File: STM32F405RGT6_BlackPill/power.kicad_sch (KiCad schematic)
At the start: 12 parts, among them U3 TLV62569DBV

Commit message: Essential part of the BOM fill
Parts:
- C300: renamed from C17; LCSC link https://www.lcsc.com/product-detail/Multilayer-Ceramic-Capa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 -> (none); Manufacturer Samwha Capacitor -> (none); Manufacturer Part Number CS1608Y5V105Z160NRB -> (none)
- C301: renamed from C18; LCSC link https://www.lcsc.com/product-detail/Multilayer-Ceramic-Capa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 -> (none); Manufacturer Samwha Capacitor -> (none); Manufacturer Part Number CS1608Y5V105Z160NRB -> (none)
- C302: renamed from C19; LCSC link https://www.lcsc.com/product-detail/Multilayer-Ceramic-Capa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 -> (none); Manufacturer Samwha Capacitor -> (none); Manufacturer Part Number CS2012X5R226M160NRE -> (none)
- C303: renamed from C22; LCSC link https://www.lcsc.com/product-detail/Multilayer-Ceramic-Capa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 -> (none); Manufacturer Samwha Capacitor -> (none); Manufacturer Part Number CS2012X5R226M160NRE -> (none)
- C304: renamed from C23; now not fitted
- D300: renamed from D4; value GREEN -> LED; LCSC link https://www.lcsc.com/product-detail/LED-Indication-Discrete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 -> (none); Manufacturer Amicc -> (none); Manufacturer Part Number A-SP192DGHC-C01-4T -> (none)
- L300: renamed from L3; footprint Capacitor_SMD:C_0402_1005Metric -> Inductor_SMD:L_0402_1005Metric; LCSC link https://www.lcsc.com/product-detail/Multilayer-Ceramic-Capa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 -> (none); Manufacturer TDK -> (none); Manufacturer Part Number CGA2B3X7R1H103M050BE -> (none)
- L301: renamed from L4; footprint PhilsLab_Footprints_KiCad6:MWSA0603S -> BlackPill:MWSA0603S; DigiKey Part Number (none) -> 3442-MWSA0603S-150MTDKR-ND; LCSC link https://www.lcsc.com/product-detail/Power-Inductors_Sunlord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 -> (none); Manufacturer Sunlord -> Shenzhen Sunlord Electronics Co., Ltd.; Manufacturer Part Number MWSA0603S-150MT -> (none); Manufacturer Product Number (none) -> MWSA0603S-150MT
- R300: renamed from R10; LCSC link https://www.lcsc.com/product-detail/Chip-Resistor-Surface-M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 -> (none); Manufacturer UNI-ROYAL(Uniroyal Elec) -> (none); Manufacturer Part Number 0402WGJ0104TCE -> (none)
- R301: renamed from R11; LCSC link https://www.lcsc.com/product-detail/Chip-Resistor-Surface-M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 -> (none); Manufacturer UNI-ROYAL(Uniroyal Elec) -> (none); Manufacturer Part Number 0402WGF2202TCE -> (none)
- R302: renamed from R12; LCSC link https://www.lcsc.com/product-detail/Chip-Resistor-Surface-M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 -> (none); Manufacturer UNI-ROYAL(Uniroyal Elec) -> (none); Manufacturer Part Number 0402WGF1001TCE -> (none)
- U300: renamed from U3; DigiKey Part Number (none) -> 296-47360-6-ND; LCSC link https://www.lcsc.com/product-detail/DC-DC-Converters_Texas-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 -> (none); Manufacturer Part Number TLV62569DBVR -> (none); Manufacturer Product Number (none) -> TLV62569DBVR

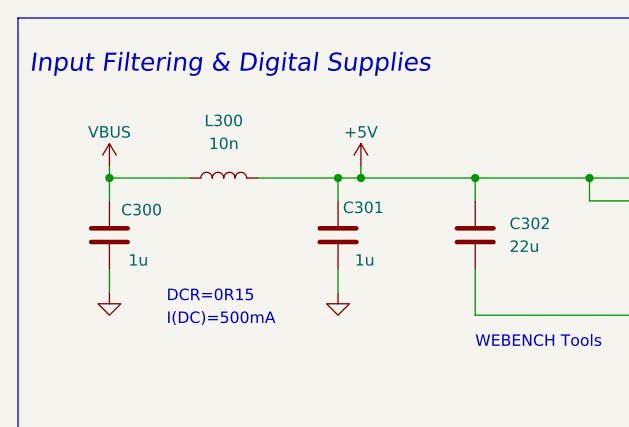
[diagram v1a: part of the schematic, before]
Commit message: BOM table fill
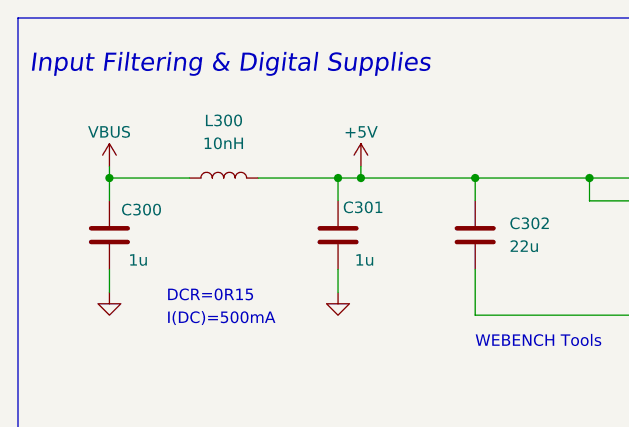
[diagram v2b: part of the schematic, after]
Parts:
- C300, C301: DigiKey Part Number (none) -> 1276-1946-6-ND; Manufacturer (none) -> Samsung Electro-Mechanics; Manufacturer Product Number (none) -> CL10B105KP8NNNC
- C302, C303: DigiKey Part Number (none) -> 1276-6687-6-ND; Manufacturer (none) -> Samsung Electro-Mechanics; Manufacturer Product Number (none) -> CL21A226KQCLRNC
- D300: DigiKey Part Number (none) -> 732-4971-6-ND; Manufacturer (none) -> Würth Elektronik; Manufacturer Product Number (none) -> 150060GS75000
- L300: value 10n -> 10nH; DigiKey Part Number (none) -> 712-LRC0402CJ10NGV001TDKR-ND; Manufacturer (none) -> Johanson Technology Inc.; Manufacturer Product Number (none) -> LRC0402CJ10NGV001T
- R300: DigiKey Part Number (none) -> P100KLDKR-ND; Manufacturer (none) -> Panasonic Electronic Components; Manufacturer Product Number (none) -> ERJ-2RKF1003X
- R301: DigiKey Part Number (none) -> P22.0KLDKR-ND; Manufacturer (none) -> Panasonic Electronic Components; Manufacturer Product Number (none) -> ERJ-2RKF2202X
- R302: DigiKey Part Number (none) -> P1.00KLDKR-ND; Manufacturer (none) -> Panasonic Electronic Components; Manufacturer Product Number (none) -> ERJ-2RKF1001X
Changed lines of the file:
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@@
 			)
 		)
-		(property "Manufacturer" ""
+		(property "Manufacturer" "Samsung Electro-Mechanics"
 			(at 33.02 43.18 0)
 			(effects
@@
 			)
 		)
-		(property "DigiKey Part Number" ""
+		(property "DigiKey Part Number" "1276-1946-6-ND"
+			(at 33.02 43.18 0)
+			(effects
+				(font
+					(size 1.27 1.27)
+				)
+				(hide yes)
+			)
+		)
+		(property "Manufacturer Product Number" "CL10B105KP8NNNC"
 			(at 33.02 43.18 0)
 			(effects
@@
 			)
 		)
-		(property "Manufacturer" ""
+		(property "Manufacturer" "Panasonic Electronic Components"
 			(at 187.96 46.99 0)
 			(effects
@@
 			)
 		)
-		(property "DigiKey Part Number" ""
+		(property "DigiKey Part Number" "P1.00KLDKR-ND"
+			(at 187.96 46.99 0)
+			(effects
+				(font
+					(size 1.27 1.27)
+				)
+				(hide yes)
+			)
+		)
+		(property "Manufacturer Product Number" "ERJ-2RKF1001X"
 			(at 187.96 46.99 0)
 			(effects
@@
 			)
 		)
-		(property "Manufacturer" ""
+		(property "Manufacturer" "Panasonic Electronic Components"
 			(at 149.86 43.18 0)
 			(effects
@@
 			)
 		)
-		(property "DigiKey Part Number" ""
+		(property "DigiKey Part Number" "P100KLDKR-ND"
+			(at 149.86 43.18 0)
+			(effects
+				(font
+					(size 1.27 1.27)
+				)
+				(hide yes)
+			)
+		)
+		(property "Manufacturer Product Number" "ERJ-2RKF1003X"
 			(at 149.86 43.18 0)
 			(effects
@@
 			)
 		)
-		(property "Manufacturer" ""
+		(property "Manufacturer" "Samsung Electro-Mechanics"
 			(at 73.66 43.18 0)
 			(effects
@@
 			)
 		)
-		(property "DigiKey Part Number" ""
+		(property "DigiKey Part Number" "1276-6687-6-ND"
+			(at 73.66 43.18 0)
+			(effects
+				(font
+					(size 1.27 1.27)
+				)
+				(hide yes)
+			)
+		)
+		(property "Manufacturer Product Number" "CL21A226KQCLRNC"
 			(at 73.66 43.18 0)
 			(effects
@@
 			)
 		)
-		(property "Manufacturer" ""
+		(property "Manufacturer" "Samsung Electro-Mechanics"
 			(at 132.08 43.18 0)
 			(effects
@@
 			)
 		)
-		(property "DigiKey Part Number" ""
+		(property "DigiKey Part Number" "1276-6687-6-ND"
+			(at 132.08 43.18 0)
+			(effects
+				(font
+					(size 1.27 1.27)
+				)
+				(hide yes)
+			)
+		)
+		(property "Manufacturer Product Number" "CL21A226KQCLRNC"
 			(at 132.08 43.18 0)
 			(effects
@@
 			)
 		)
-		(property "Manufacturer" ""
+		(property "Manufacturer" "Samsung Electro-Mechanics"
 			(at 58.42 43.18 0)
 			(effects
@@
 			)
 		)
-		(property "DigiKey Part Number" ""
+		(property "DigiKey Part Number" "1276-1946-6-ND"
+			(at 58.42 43.18 0)
+			(effects
+				(font
+					(size 1.27 1.27)
+				)
+				(hide yes)
+			)
+		)
+		(property "Manufacturer Product Number" "CL10B105KP8NNNC"
 			(at 58.42 43.18 0)
 			(effects
@@
 			)
 		)
-		(property "Manufacturer" ""
+		(property "Manufacturer" "Würth Elektronik"
 			(at 175.26 36.83 0)
 			(effects
@@
 			)
 		)
-		(property "DigiKey Part Number" ""
+		(property "DigiKey Part Number" "732-4971-6-ND"
+			(at 175.26 36.83 0)
+			(effects
+				(font
+					(size 1.27 1.27)
+				)
+				(hide yes)
+			)
+		)
+		(property "Manufacturer Product Number" "150060GS75000"
 			(at 175.26 36.83 0)
 			(effects
@@
 			)
 		)
-		(property "Value" "10n"
+		(property "Value" "10nH"
 			(at 45.72 33.02 90)
 			(effects
@@
 			)
 		)
-		(property "Manufacturer" ""
+		(property "Manufacturer" "Johanson Technology Inc."
 			(at 45.72 36.83 0)
 			(effects
@@
 			)
 		)
-		(property "DigiKey Part Number" ""
+		(property "DigiKey Part Number" "712-LRC0402CJ10NGV001TDKR-ND"
+			(at 45.72 36.83 0)
+			(effects
+				(font
+					(size 1.27 1.27)
+				)
+				(hide yes)
+			)
+		)
+		(property "Manufacturer Product Number" "LRC0402CJ10NGV001T"
 			(at 45.72 36.83 0)
 			(effects
@@
 			)
 		)
-		(property "Manufacturer" ""
+		(property "Manufacturer" "Panasonic Electronic Components"
 			(at 149.86 57.15 0)
 			(effects
@@
 			)
 		)
-		(property "DigiKey Part Number" ""
+		(property "DigiKey Part Number" "P22.0KLDKR-ND"
 			(at 149.86 57.15 0)
 			(effects
+				(font
+					(size 1.27 1.27)
+				)
+				(hide yes)
+			)
+		)
+		(property "Manufacturer Product Number" "ERJ-2RKF2202X"
+			(at 149.86 57.15 0)
+			(effects

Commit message: Signal routing (bottom part)
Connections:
- net +3V3 renamed +3.3V
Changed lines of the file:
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@@
+	)
+	(symbol
+		(lib_id "power:+3.3V")
+		(at 165.1 34.29 0)
+		(unit 1)
+		(exclude_from_sim no)
+		(in_bom yes)
+		(on_board yes)
+		(dnp no)
+		(fields_autoplaced yes)
+		(property "Reference" "#PWR037"
+			(at 165.1 38.1 0)
+			(effects
+				(font
+					(size 1.27 1.27)
+				)
+				(hide yes)
+			)
+		)
+		(property "Value" "+3.3V"
+			(at 165.1 29.21 0)
+			(effects
+				(font
+					(size 1.27 1.27)
+				)
+			)
+		)
+		(property "Footprint" ""
+			(at 165.1 34.29 0)
+			(effects
+				(font
+					(size 1.27 1.27)
+				)
+				(hide yes)
+			)
+		)
+		(property "Datasheet" ""
+			(at 165.1 34.29 0)
+			(effects
+				(font
+					(size 1.27 1.27)
+				)
+				(hide yes)
+			)
+		)
+		(property "Description" "Power symbol creates a global label with name \"+3.3V\""
+			(at 165.1 34.29 0)
+			(effects
+				(font
+					(size 1.27 1.27)
+				)
+				(hide yes)
+			)
+		)
+		(pin "1"
+		)
+		(instances
+			(project "STM32F405RGT6_BlackPill"
+				(path "/cae5b0ba-cc42-4347-bdfb-a704c1b808ff/2ee95013-77be-4b2e-9d54-3c8eff576e64"
+					(reference "#PWR037")
+					(unit 1)
+				)
+			)
+		)
 	)
 	(symbol
@@
 					(unit 1)
 				)
-			)
-		)
-	)
-	(symbol
-		(lib_id "power:+3V3")
-		(at 165.1 34.29 0)
-		(unit 1)
-		(exclude_from_sim no)
-		(in_bom yes)
-		(on_board yes)
-		(dnp no)
-		(property "Reference" "#PWR037"
-			(at 165.1 38.1 0)
-			(effects
-				(font
-					(size 1.27 1.27)
-				)
-				(hide yes)
-			)
-		)
-		(property "Value" "+3V3"
-			(at 165.1 30.48 0)
-			(effects
-				(font
-					(size 1.27 1.27)
-				)
-			)
-		)
-		(property "Footprint" ""
-			(at 165.1 34.29 0)
-			(effects
-				(font
-					(size 1.27 1.27)
-				)
-				(hide yes)
-			)
-		)
-		(property "Datasheet" ""
-			(at 165.1 34.29 0)
-			(effects
-				(font
-					(size 1.27 1.27)
-				)
-				(hide yes)
-			)
-		)
-		(property "Description" ""
-			(at 165.1 34.29 0)
-			(effects
-				(font
-					(size 1.27 1.27)
-				)
-				(hide yes)
-			)
-		)
-		(pin "1"
-		)
-		(instances
-			(project "STM32F405RGT6_BlackPill"
-				(path "/cae5b0ba-cc42-4347-bdfb-a704c1b808ff/2ee95013-77be-4b2e-9d54-3c8eff576e64"
-					(reference "#PWR037")
-					(unit 1)
-				)

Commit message: Production files JLCPCB
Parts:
- C302, C303: Manufacturer Product Number CL21A226KQCLRNC -> CL21A226MQQNNNE
- D300: Manufacturer Würth Elektronik -> Hubei KENTO Elec; Manufacturer Product Number 150060GS75000 -> KT-0603R
- L300: Manufacturer Johanson Technology Inc. -> Murata Electronics; Manufacturer Product Number LRC0402CJ10NGV001T -> LQG15HS10NJ02D
- L301: Manufacturer Shenzhen Sunlord Electronics Co., Ltd. -> cjiang (Changjiang Microelectronics Tech); Manufacturer Product Number MWSA0603S-150MT -> FXL0630-150-M
- R300: Manufacturer Panasonic Electronic Components -> UNI-ROYAL(Uniroyal Elec); Manufacturer Product Number ERJ-2RKF1003X -> 0402WGF1003TCE
- R301: Manufacturer Panasonic Electronic Components -> UNI-ROYAL(Uniroyal Elec); Manufacturer Product Number ERJ-2RKF2202X -> 0402WGF2202TCE
- R302: Manufacturer Panasonic Electronic Components -> UNI-ROYAL(Uniroyal Elec); Manufacturer Product Number ERJ-2RKF1001X -> 0402WGF1001TCE
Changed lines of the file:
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@@
 			)
 		)
-		(property "Manufacturer" "Panasonic Electronic Components"
+		(property "Manufacturer" "UNI-ROYAL(Uniroyal Elec)"
 			(at 187.96 46.99 0)
 			(effects
@@
 			)
 		)
-		(property "Manufacturer Product Number" "ERJ-2RKF1001X"
+		(property "Manufacturer Product Number" "0402WGF1001TCE"
 			(at 187.96 46.99 0)
 			(effects
@@
 			)
 		)
-		(property "Manufacturer" "Panasonic Electronic Components"
+		(property "Manufacturer" "UNI-ROYAL(Uniroyal Elec)"
 			(at 149.86 43.18 0)
 			(effects
@@
 			)
 		)
-		(property "Manufacturer Product Number" "ERJ-2RKF1003X"
+		(property "Manufacturer Product Number" "0402WGF1003TCE"
 			(at 149.86 43.18 0)
 			(effects
@@
 			)
 		)
-		(property "Manufacturer Product Number" "CL21A226KQCLRNC"
+		(property "Manufacturer Product Number" "CL21A226MQQNNNE"
 			(at 73.66 43.18 0)
 			(effects
@@
 			)
 		)
-		(property "Manufacturer Product Number" "CL21A226KQCLRNC"
+		(property "Manufacturer Product Number" "CL21A226MQQNNNE"
 			(at 132.08 43.18 0)
 			(effects
@@
 			)
 		)
-		(property "Manufacturer" "Würth Elektronik"
+		(property "Manufacturer" "Hubei KENTO Elec"
 			(at 175.26 36.83 0)
 			(effects
@@
 			)
 		)
-		(property "Manufacturer Product Number" "150060GS75000"
+		(property "Manufacturer Product Number" "KT-0603R"
 			(at 175.26 36.83 0)
 			(effects
@@
 			)
 		)
-		(property "Manufacturer" "Johanson Technology Inc."
+		(property "Manufacturer" "Murata Electronics"
 			(at 45.72 36.83 0)
 			(effects
@@
 			)
 		)
-		(property "Manufacturer Product Number" "LRC0402CJ10NGV001T"
+		(property "Manufacturer Product Number" "LQG15HS10NJ02D"
 			(at 45.72 36.83 0)
 			(effects
@@
 			)
 		)
-		(property "Manufacturer" "Panasonic Electronic Components"
+		(property "Manufacturer" "UNI-ROYAL(Uniroyal Elec)"
 			(at 149.86 57.15 0)
 			(effects
@@
 			)
 		)
-		(property "Manufacturer Product Number" "ERJ-2RKF2202X"
+		(property "Manufacturer Product Number" "0402WGF2202TCE"
 			(at 149.86 57.15 0)
 			(effects
@@
 			)
 		)
-		(property "Manufacturer" "Shenzhen Sunlord Electronics Co., Ltd."
+		(property "Manufacturer" "cjiang (Changjiang Microelectronics Tech)"
 			(at 120.65 36.83 0)
 			(effects
@@
 			)
 		)
-		(property "Manufacturer Product Number" "MWSA0603S-150MT"
+		(property "Manufacturer Product Number" "FXL0630-150-M"
 			(at 120.65 36.83 0)
 			(effects
